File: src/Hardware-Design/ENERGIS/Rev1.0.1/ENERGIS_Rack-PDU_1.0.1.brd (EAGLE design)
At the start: 210 x 108 mm, 428 parts, among them IC1 MP2315GJ-Z, IC10 HLW8032, IC11 HLW8032, IC12 HLW8032, IC13 MP150GJ, IC14 HLW8032, IC15 RP2040, IC16 HLW8032, IC17 MCP6001RT-I/OT, IC18 W25Q128JVPIQ, IC19 CAT24C256HU4IGT3, IC2 MP2315GJ-Z, IC20 W5500, IC21 MIC5504-3.3YM5, IC22 MCP6001RT-I/OT, IC3 ULN2803AFWG, IC4 MCP23017T-E/ML, IC5 MP150GJ, IC6 HLW8032, IC7 HLW8032, IC8 HLW8032, IC9 SN74HC151PWR, J10 0R 1%, J2 JP, J7 JP, J8 0R 1%, J9 0R 1%, K1 G2RL-1A-E DC12, K2 G2RL-1A-E DC12, K3 G2RL-1A-E DC12, K4 G2RL-1A-E DC12, K5 G2RL-1A-E DC12, K6 G2RL-1A-E DC12, K7 G2RL-1A-E DC12, K8 G2RL-1A-E DC12, P12ON Green, P3ON Green, P5ON Green, SW3 TP, X1 ABM8-272-T3 12MHz, X2 25MHz

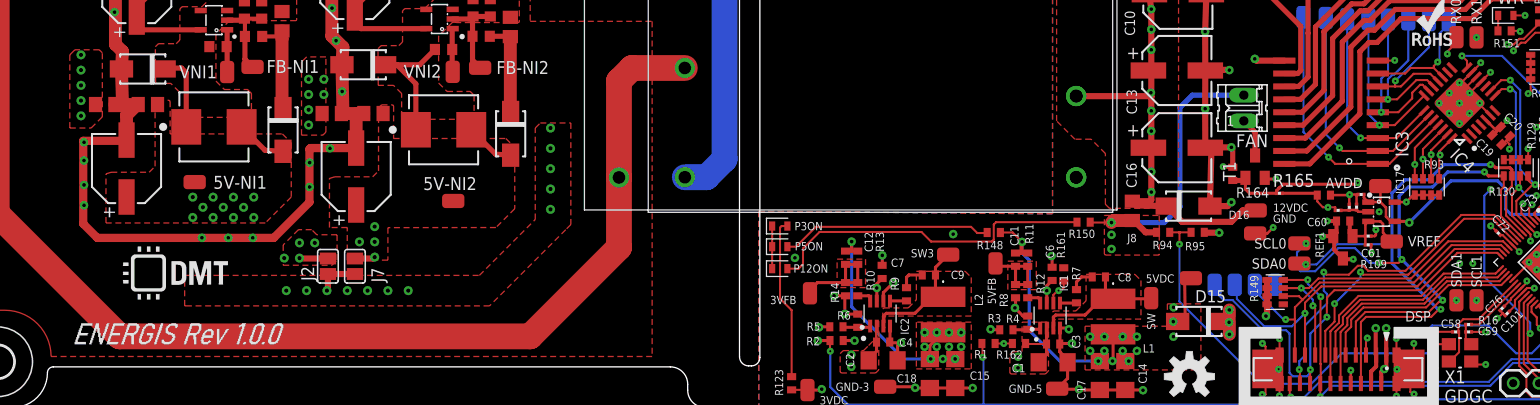
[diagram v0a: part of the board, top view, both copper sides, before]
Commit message: Add software ESD protection to button control and port expanders. Design sheet metal shielding around electronics. Add ethernet test
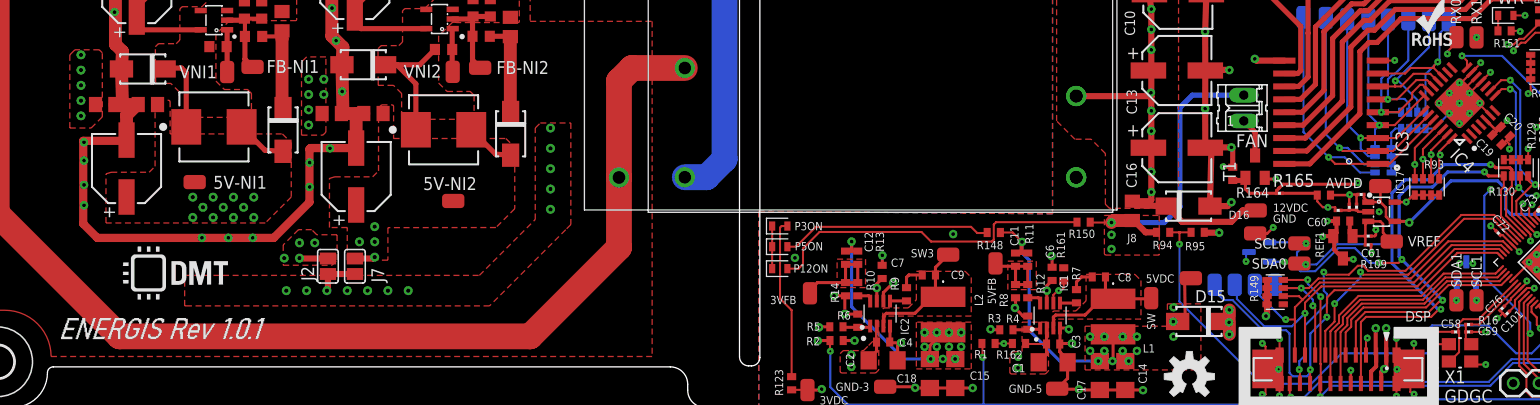
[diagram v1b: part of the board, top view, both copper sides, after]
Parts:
- added D17, D18: RCLAMP0582BQTCT, ds_diode:SOT-523
- added RN1, RN2: 100K 1%, ds_resistor:_0603X4-1206
- R17, R18, R19, R20, R21, R22, R23, R24: value 330R 1% 1W -> 0R 1%
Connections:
- net GND: now also D17.3, D18.3, RN1.A1, RN1.B1, RN1.C1, RN1.D1, RN2.A1, RN2.B1, RN2.C1, RN2.D1
- net I2C0_SCL: now also D17.1
- net I2C0_SDA: now also D17.2
- net I2C1_SCL: now also D18.1
- net I2C1_SDA: now also D18.2
- net REL_0: now also RN1.A2
- net REL_1: now also RN1.B2
- net REL_2: now also RN1.C2
- net REL_3: now also RN1.D2
- net REL_4: now also RN2.A2
- net REL_5: now also RN2.B2
- net REL_6: now also RN2.C2
- net REL_7: now also RN2.D2
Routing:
- net GND: track 279.3 -> 292.2 mm, vias 159 -> 160
- net REL_0: track 12.3 -> 17.7 mm
- net REL_7: track 27.2 -> 32.4 mm
- net REL_6: track 23.7 -> 27.9 mm
- net REL_1: track 14.7 -> 18.8 mm
- net I2C0_SCL: track 58.6 -> 62.2 mm
- net REL_2: track 15.3 -> 18.4 mm
- net I2C0_SDA: track 58.4 -> 61.4 mm, vias 3 -> 4
- net REL_5: track 19.6 -> 22.4 mm
- net REL_4: track 16.6 -> 19.1 mm
- net REL_3: track 16.1 -> 18.1 mm
- net I2C1_SCL: track 32.6 -> 34.3 mm
- net I2C1_SDA: track 35.1 -> 36.8 mm
